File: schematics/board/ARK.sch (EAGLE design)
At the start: 85 parts, among them IC2 STM32F103C8T

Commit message: Готова схема платы АРК
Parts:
- removed 3,3µH: 3,3µ, CanCubeSat:B82472G6
- removed 3,3µH1: 3,3µH, CanCubeSat:B82472G6
- removed AD5272#2: AD5272, CanCubeSat:AD5272
- removed C29: 1µ, rcl:C-USC0603
- removed C3: 470nF, rcl:C-EUC0603
- removed C40, C41, C49, C50, C56: 0,1µ, rcl:C-USC0603
- removed C44, C52: 680p, rcl:C-USC0603
- removed C45, C53: 4.7µ, rcl:C-USC1206
- removed C46: 3,3n, rcl:C-USC0603
- removed C47, C54: 150µ, CanCubeSat:ECAPECAP150
- removed C48, C55: 220µ, CanCubeSat:ECAPECAP220
- removed C57: 10µ, rcl:C-USC1206
- removed INVERT: INVERTER., CanCubeSat:INVERTER.
- removed LED_G1, LED_G2, LED_R1, LED_R2: (no value), led:LEDCHIPLED_0603
- removed OPA: OPA333, CanCubeSat:OPA333
- removed R1: 91K, resistor:R-US_R0603
- removed R100, R32, R33, R57: 2k, resistor:R-US_R0603
- removed R28, R30, R67, R68, R69: 150k, resistor:R-US_R0603
- removed R3: 14K3, resistor:R-US_R0603
- removed R4: 120k, resistor:R-US_R0603
- removed R5: 430k, resistor:R-US_R0603
- removed R65: 1M, resistor:R-US_R0603
- removed R66: 10k, resistor:R-US_R0603
- removed R7: 680k, resistor:R-US_R0603
- removed REF3033: REF3033, CanCubeSat:REF3033
- removed U$1: MF-R400, CanCubeSat:MF-R400
- removed U$23, U$59: LTC31191, CanCubeSat:LTC31191
- removed VR-FB: 3314G-1-504E, CanCubeSat:3314G-1-504E
- removed VR-RUN: 3313J-1-205E, CanCubeSat:3313J-1-205E
- added 3362H, 3362H1: 20k, CanCubeSat:3362H
- added 3362P, 3362P1, 3362P4: 1k, CanCubeSat:3362P-1-502LF
- added 3362P2, 3362P5: 5k, CanCubeSat:3362P-1-502LF
- added 3362P3: 500R, CanCubeSat:3362P-1-502LF
- added C1.C, C1.D, C2B.C, C2B.D: 100nF, rcl:C-EUC0603
- added C2A.C, C2A.D: 22µF, rcl:C-EUC1206
- added C3.C, C3.D, C4A.C, C4A.D, C5.C, C5.D: 1µF, rcl:C-EUC0603
- added C4B.C, C4B.D: 1000µF, CanCubeSat:ECAPECAP1000
- added C6.C, C6.D: 10nF, rcl:C-EUC0603
- added C7.C, C7.D, C8.C, C8.D: (10nF), rcl:C-EUC0603
- added INVERT1: INVERTER., CanCubeSat:INVERTER.
- added L1.C, L1.D: 10µH, CanCubeSat:L_10MKH
- added OPA1, OPA2, OPA3: OPA333, CanCubeSat:OPA333
- added PB1, PB2, PB3, PB4, PB6, PB7: (no value), led:LEDCHIPLED_0603
- added R1.C, R1.D: 62k, rcl:R-US_R0603
- added R10, R12, R14, R15, R2, R21, R25, R29, R31, R34, R35, R36, R37, R38, R39, R40, R41, R42, R45, R48, R49, R6, R8, R9: 10k, resistor:R-US_R0603
- added R10.C, R10.D: 11k, rcl:R-US_R0603
- added R11: 34k8, resistor:R-US_R0603
- added R11.C, R11.D, R12.C, R12.D, R13.C, R13.D, R14.C, R14.D, R15.C, R15.D: 100k, rcl:R-US_R0603
- added R13: 91k, resistor:R-US_R0603
- added R16, R17, R18, R22, R23, R24, R26, R43: 2k, resistor:R-US_R0603
- added R16.C, R16.D, R17.C, R17.D, R2.C, R2.D, R6.C, R6.D: 10k, rcl:R-US_R0603
- added R18.C, R18.D: 51k, rcl:R-US_R0603
- added R19, R20: 51k, resistor:R-US_R0603
- added R19.C, R19.D: (1M), rcl:R-US_R0603
- added R44: 1k, resistor:R-US_R0603
- added R46: 24k9, resistor:R-US_R0603
- added R47: 620k, resistor:R-US_R0603
- added R5.C, R5.D: 191k, rcl:R-US_R0603
- added R7.C, R7.D: 17k8, rcl:R-US_R0603
- added R8.C, R8.D: (10k), rcl:R-US_R0603
- added R9.C, R9.D: 200k, rcl:R-US_R0603
- added ROZE1, ROZE2, ROZE3, ROZE4: (no value), pinheadCS:PINHD-1X2
- added U$10, U$11, U$17, U$18, U$19, U$22, U$24, U$25, U$27, U$28, U$30, U$31, U$32, U$33, U$41, U$42, U$43, U$46, U$47, U$48, U$50, U$51, U$53, U$9: VIAS, CanCubeSat:VIAS
- added U$13, U$14, U$15, U$16, U$20, U$21, U$26, U$29, U$39, U$40, U$44, U$45, U$49, U$52: VIAS-CONNECT, CanCubeSat:VIAS-CONNECT
- added U$2, U$5: MP5515, CanCubeSat:MP5515
- added U$34, U$35, U$6: IRF7329PBF, CanCubeSat:IRF7329PBF
- added U$36, U$37: IRF7905PBF, CanCubeSat:IRF7905PBF
- added U$38: SI2302CDS, CanCubeSat:SI2302CDS
- added U$7, U$8: SMP100LC-8, CanCubeSat:SMP100LC-8
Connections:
- removed net 3V3-STAB: IC2.VDDA, INVERT.VCC, OPA.V+, R4.1, REF3033.OUT
- removed net 90: R65.1, R66.2, R67.2, U$59.MPPC
- removed net DPD_RST: AD5272#2.RESET, IC2.PB15
- removed net GND-OUT: JP1.11, JP1.12, U$1.P$2, U$12.3, U$12.5, U$12.7, U$12.9
- removed net N$129: C41.2, U$59.BST2
- removed net N$131: 3,3µH.2, C40.1, U$59.SW1
- removed net N$132: 3,3µH.1, C41.1, U$59.SW2
- removed net N$135: R69.1, U$59.VC
- removed net N$136: C44.1, R69.2
- removed net N$139: C46.1, R66.1
- removed net N$142: R68.2, U$59.RT
- removed net N$144: C40.2, U$59.BST1
- removed net N$161: IC2.PB5, R81.1
- removed net N$2: OPA.IN+, R4.2, R5.2, R7.2
- removed net N$215: AD5272#2.VDD, C53.1, C56.1, C57.1, LED_G2.A, U$23.MPPC, U$23.SVCC, U$23.VCC
- removed net N$234: C45.1, LED_G1.A, U$59.SVCC, U$59.VCC
- removed net N$3: AD5272#2.A, R1.2, U$23.FB
- removed net N$48: AD5272#2.VSS, AD5272#2.W, C29.2, R3.1
- removed net N$51: AD5272#2.CAP, C29.1
- removed net N$77: 3,3µH1.2, C49.1, U$23.SW1
- removed net N$78: 3,3µH1.1, C50.1, U$23.SW2
- removed net N$79: R28.2, U$23.RT
- removed net N$80: C49.2, U$23.BST1
- removed net N$81: R30.1, U$23.VC
- removed net N$82: C52.1, R30.2
- removed net N$84: C50.2, U$23.BST2
- removed net N$85: LED_R1.A, R32.2
- removed net N$87: LED_R2.A, R57.2
- removed net N$89: U$59.FB, VR-FB.WIPER
- removed net N$91: LED_G1.C, R100.2
- removed net N$92: LED_G2.C, R33.2
- removed net PGOOD1: IC2.PB1, LED_R2.C, U$59.PGOOD
- removed net PGOOD2: IC2.PB0, LED_R1.C, U$23.PGOOD
- removed net RUN: OPA.IN-, VR-RUN.WIPER
- new net 0V8: 3362P.WIPER, OPA2.IN+, U$32.1
- new net AGND: C1.C.1, C1.D.1, C3.C.2, C3.D.2, C6.C.2, C6.D.2, C7.C.2, C7.D.2, C8.C.2, C8.D.2, R10.C.2, R10.D.2, R13.C.1, R13.D.1, R18.C.2, R18.D.2, R19.C.2, R19.D.2, R2.C.2, R2.D.2, R6.C.2, R6.D.2, R7.C.1, R7.D.1, U$2.AGND, U$39.2, U$5.AGND
- new net DC-DC: IC2.PA15, R42.2, U$38.G
- new net FBB-C: R15.2, U$2.FBB
- new net FBB-D: R25.2, U$5.FBB
- new net INT-C: IC2.PB4, R15.C.1, U$2.INT
- new net INT-D: IC2.PA8, R15.D.1, U$5.INT
- new net LED: IC2.PB0, R81.1
- new net N$10: R1.C.2, R2.C.1, U$2.DET
- new net N$100: 3362P5.WIPER, OPA1.IN-, U$48.1
- new net N$101: R45.2, U$44.1, U$47.1
- new net N$102: R46.1, U$45.2, U$46.1
- new net N$104: 3362H1.CCW, R48.1
- new net N$105: 3362H1.WIPER, OPA1.IN+, U$51.1
- new net N$106: 3362H1.CW, R47.2
- new net N$108: R47.1, U$49.2, U$50.1
- new net N$109: R48.2, U$52.2, U$53.1
- new net N$11: R10.C.1, R9.C.2, U$2.OVP
- new net N$12: C8.C.1, U$2.DVDT
- new net N$13: R18.C.1, U$2.ICH
- new net N$15: R19.C.1, U$2.TEMP
- new net N$16: R13.C.2, U$2.SAS
- new net N$18: C6.C.1, U$2.CST
- new net N$19: C4A.C.2, C4B.C.1, R5.C.1, R8.C.1, U$2.STRG
- new net N$20: C5.C.2, U$2.BST
- new net N$21: C5.C.1, L1.C.1, U$2.SW
- new net N$22: R5.C.2, R6.C.1, U$2.FBS
- new net N$23: R8.C.2, U$2.RTEST
- new net N$24: 3362P4.CCW, R22.1
- new net N$25: R29.2, U$36.D1, U$6.G1
- new net N$26: R17.C.1, U$2.SCL
- new net N$27: R16.C.1, U$2.SDA
- new net N$28: R35.2, U$34.G, U$37.D
- new net N$29: 3362P2.WIPER, OPA3.IN+, U$19.1
- new net N$30: R11.D.1, R12.D.2, U$5.EN
- new net N$31: R1.D.2, R2.D.1, U$5.DET
- new net N$32: R10.D.1, R9.D.2, U$5.OVP
- new net N$33: R7.D.2, U$5.ILIM
- new net N$34: C7.D.1, U$5.TPOR
- new net N$35: C8.D.1, U$5.DVDT
- new net N$36: R18.D.1, U$5.ICH
- new net N$37: R19.D.1, U$5.TEMP
- new net N$38: R13.D.2, U$5.SAS
- new net N$39: C6.D.1, U$5.CST
- new net N$40: C5.D.2, U$5.BST
- new net N$41: C5.D.1, L1.D.1, U$5.SW
- new net N$42: R5.D.2, R6.D.1, U$5.FBS
- new net N$43: R8.D.2, U$5.RTEST
- new net N$44: C4A.D.2, C4B.D.1, R5.D.1, R8.D.1, U$5.STRG
- new net N$46: U$35.D, U$35.D1
- new net N$47: R17.D.1, U$5.SCL
- new net N$49: R16.D.1, U$5.SDA
- new net N$5: R34.2, U$34.G1, U$37.D1
- new net N$52: OPA2.OUT, R15.1, U$29.1
- new net N$53: 3362H.WIPER, OPA2.IN-, U$28.1
- new net N$54: 3362H.CW, R9.2
- new net N$55: 3362H.CCW, R10.1
- new net N$56: PB1.C, R16.2
- new net N$57: 3362P.CW, R11.1
- new net N$58: 3362P.CCW, R12.2
- new net N$59: 3362P1.CW, R13.1
- new net N$6: OPA3.OUT, R25.1, U$13.1
- new net N$60: 3362P1.CCW, R14.2
- new net N$61: 3362P1.WIPER, U$25.1, U$26.1
- new net N$62: 3362P2.CW, R20.1
- new net N$63: PB2.C, R17.2
- new net N$64: 3362P2.CCW, R21.2
- new net N$65: PB3.C, R18.2
- new net N$66: 3362P4.WIPER, OPA3.IN-, U$10.1
- new net N$67: 3362P4.CW, R19.2
- new net N$68: PB4.C, R23.2
- new net N$69: PB6.C, R24.2
- new net N$7: R11.C.1, R12.C.2, U$2.EN
- new net N$70: PB7.C, R26.2
- new net N$71: R22.2, U$13.2, U$9.1
- new net N$72: R19.1, U$11.1, U$14.2
- new net N$73: R20.2, U$15.1, U$18.1
- new net N$74: R21.1, U$16.2, U$17.1
- new net N$75: R13.2, U$21.2, U$24.1
- new net N$76: R14.1, U$20.1, U$22.1
- new net N$8: R7.C.2, U$2.ILIM
- new net N$83: R9.1, U$26.2, U$27.1
- new net N$86: R10.2, U$29.2, U$30.1
- new net N$88: R31.2, U$36.D, U$6.G
- new net N$9: C7.C.1, U$2.TPOR
- new net N$90: 3362P3.CW, R43.1
- new net N$93: 3362P3.CCW, R44.2
- new net N$94: 3362P3.WIPER, U$43.1, U$52.1
- new net N$95: R40.2, R41.2, U$35.G, U$35.G1, U$38.D
- new net N$96: R43.2, U$39.1, U$42.1
- new net N$97: R44.1, U$40.2, U$41.1
- new net N$98: 3362P5.CW, R45.1
- new net N$99: 3362P5.CCW, R46.2
- new net PFI-C: IC2.PB6, PB1.A, R14.C.2, U$2.PFI
- new net PFI-D: IC2.PB14, PB4.A, R14.D.2, U$5.PFI
- new net PGB-C: IC2.PB7, PB3.A, U$2.PGB
- new net PGB-D: IC2.PB15, PB7.A, U$5.PGB
- new net PGS-C: IC2.PB5, PB2.A, U$2.PGS
- new net PGS-D: IC2.PB13, PB6.A, U$5.PGS
- new net ROZE-1: IC2.PA7, R2.1, ROZE1.1
- new net ROZE-2: IC2.PB3, R6.1, ROZE2.1
- new net ROZE-3: IC2.PA11, R8.1, ROZE3.1
- new net ROZE-4: IC2.PB1, R49.1, ROZE4.1
- new net VB-C: C2A.C.1, C2B.C.1, R12.C.1, R31.1, U$2.VB, U$6.S
- new net VB-D: C2A.D.1, C2B.D.1, R12.D.1, R35.1, U$34.S, U$5.VB
- new net VBO-C: L1.C.2, U$2.VBO
- new net VBO-D: L1.D.2, U$5.VBO
- new net VCC-C: C3.C.1, R14.C.1, R15.C.2, R16.C.2, R17.C.2, U$2.VCC
- new net VCC-D: C3.D.1, R14.D.1, R15.D.2, R16.D.2, R17.D.2, U$5.VCC
- new net VIN-C: C1.C.2, R1.C.1, R11.C.2, R9.C.1, U$2.VIN, U$6.D1, U$7.C
- new net VIN-D: C1.D.2, R1.D.1, R11.D.2, R9.D.1, U$34.D1, U$5.VIN, U$8.C
- net 1W: now also IC2.PA5; no longer IC2.PA7
- net 3V3: now also IC2.VDDA, INVERT1.VCC, OPA1.V+, OPA2.V+, OPA3.V+, R11.2, R2.2, R49.2, R6.2, R8.2, U$31.1, U$40.1
- net A: now also INVERT1.A, OPA1.OUT, R38.2, R39.2, U$37.G, U$37.G1, U$49.1; no longer INVERT.A, OPA.OUT, R32.1, R7.1, U$23.RUN
- net BMS+: now also R34.1, R40.1, U$14.1, U$34.S1, U$35.S1, U$6.D; no longer C3.2, REF3033.IN
- net BMS1: now also IC2.PA1; no longer IC2.PA6
- net BMS2: now also IC2.PA2; no longer IC2.PA5
- net BMS3: now also IC2.PC15; no longer IC2.PA4
- net BMS4: now also IC2.PA0-WKUP; no longer IC2.PA3
- net BMS5: now also IC2.PC13; no longer IC2.PA2
- net BMS6: now also IC2.PC14; no longer IC2.PA1
- net BUS+: now also R29.1, R41.1, U$15.2, U$21.1, U$34.D, U$35.S, U$45.1, U$6.S1
- net GND: now also C2A.C.2, C2A.D.2, C2B.C.2, C2B.D.2, C4A.C.1, C4A.D.1, C4B.C.2, C4B.D.2, INVERT1.GND, JP1.11, JP1.12, OPA1.V-, OPA2.V-, OPA3.V-, R12.1, R16.1, R17.1, R18.1, R23.1, R24.1, R26.1, R36.1, R37.1, R38.1, R39.1, R42.1, ROZE1.2, ROZE2.2, ROZE3.2, ROZE4.2, U$12.3, U$12.5, U$12.7, U$12.9, U$16.1, U$20.2, U$33.1, U$36.S, U$36.S1, U$37.S, U$37.S1, U$38.S, U$44.2, U$7.A, U$8.A; no longer AD5272#2.ADDR, AD5272#2.GND, C3.1, C44.2, C45.2, C46.2, C47.2, C48.2, C52.2, C53.2, C54.2, C55.2, C56.2, C57.2, IC2.PB2, INVERT.GND, OPA.V-, R100.1, R28.1, R3.2, R33.1, R5.1, R67.1, R68.1, REF3033.GND, U$1.P$1, U$23.PGND, U$23.PWM, U$23.SGND, U$59.PGND, U$59.PWM, U$59.SGND, VR-FB.CW, VR-RUN.CW
- net INA_BMS+: no longer C47.1, C55.1, U$23.PVIN, U$23.VIN, U$59.PVOUT, VR-FB.CCW
- net INA_BUS+: no longer C48.1, C54.1, R1.1, R65.2, U$23.PVOUT, U$59.PVIN, U$59.VIN, VR-RUN.CCW
- net SCL: no longer AD5272#2.SCL
- net SDA: no longer AD5272#2.SDA
- net TIME: now also IC2.PA3; no longer IC2.PB6
- net Y: now also INVERT1.Y, R36.2, R37.2, U$36.G, U$36.G1; no longer INVERT.Y, R57.1, U$59.RUN
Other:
- note added: "Выключатель АРКа"
- note removed: "Источник опорного напряжения 3V3-STUB"
- note removed: "Предохранитель и выключатель АРКа"
- moved on the sheet: C11, C4, LD1117S33, R101, R102, SWITCH

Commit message: Начата разводка платы АРК
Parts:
- C4A.C, C4A.D: device rcl:C-EUC0603 -> rcl:C-EUC1206
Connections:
- new net N$2: IC2.PB1
- new net N$3: IC2.PB2
- net 1W: now also IC2.PA4; no longer IC2.PA5
- net AGND: no longer C1.C.1, C1.D.1
- net BMS+: no longer R34.1, R40.1, U$34.S1, U$35.S1, U$6.D
- net BUS+: no longer R29.1, R41.1, U$34.D, U$35.S, U$6.S1
- net GND: now also C1.C.1, C1.D.1, U$2.PGND, U$5.PGND
- net INA_BMS+: now also R34.1, R40.1, U$34.S1, U$35.S1, U$6.D
- net INA_BUS+: now also R29.1, R41.1, U$34.D, U$35.S, U$6.S1
- net INT-C: now also IC2.PB13; no longer IC2.PB4
- net INT-D: now also IC2.PB4; no longer IC2.PA8
- net LED: now also IC2.PB12; no longer IC2.PB0
- net PFI-C: now also IC2.PA8; no longer IC2.PB6
- net PFI-D: now also IC2.PB7; no longer IC2.PB14
- net PGB-C: now also IC2.PB14; no longer IC2.PB7
- net PGB-D: now also IC2.PB6; no longer IC2.PB15
- net PGS-C: now also IC2.PB15; no longer IC2.PB5
- net PGS-D: now also IC2.PB5; no longer IC2.PB13
- net ROZE-1: now also IC2.PA5; no longer IC2.PA7
- net ROZE-2: now also IC2.PA6; no longer IC2.PB3
- net ROZE-3: now also IC2.PA7; no longer IC2.PA11
- net ROZE-4: now also IC2.PB0; no longer IC2.PB1

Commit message: Разведена плата АРК
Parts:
- removed C15: 100nF, rcl:C-EUC0603
- removed R36, R37: 10k, resistor:R-US_R0603
- added R1: 10k, resistor:R-US_R0603
- added R3: 100, resistor:R-US_R0603
- R39: value 10k -> 100
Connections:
- removed net N$2: IC2.PB1
- removed net N$3: IC2.PB2
- new net C-OFF: IC2.PB1, R3.1
- new net D-OFF: IC2.PB2, R39.2
- new net N$48: R1.2, R3.2, U$36.G1, U$36.G2
- new net N$51: R38.1, R39.1, U$37.G1, U$37.G2
- net 3V3: no longer C15.1
- net A: no longer R39.2, U$37.G, U$37.G1
- net AGND: now also INVERT1.GND, OPA1.V-, OPA2.V-, OPA3.V-
- net GND: now also U$36.S2, U$37.S2; no longer C15.2, INVERT1.GND, OPA1.V-, OPA2.V-, OPA3.V-, R36.1, R37.1, R38.1, R39.1, U$36.S, U$37.S
- net INA_BMS+: now also U$34.S2, U$35.S2, U$6.D1; no longer U$34.S1, U$35.S1, U$6.D
- net INA_BUS+: now also U$34.D1, U$35.S1, U$6.S2; no longer U$34.D, U$35.S, U$6.S1
- net INT-D: now also IC2.PB5; no longer IC2.PB4
- net N$25: now also U$6.G2; no longer U$6.G1
- net N$28: now also U$34.G1, U$37.D2; no longer U$34.G, U$37.D
- net N$46: now also U$35.D2; no longer U$35.D
- net N$5: now also U$34.G2; no longer U$34.G1
- net N$88: now also U$36.D2, U$6.G1; no longer U$36.D, U$6.G
- net N$95: now also U$35.G2; no longer U$35.G
- net PFI-D: now also IC2.PB4; no longer IC2.PB7
- net PGS-D: now also IC2.PB7; no longer IC2.PB5
- net VB-C: now also U$6.S1; no longer U$6.S
- net VB-D: now also U$34.S1; no longer U$34.S
- net VIN-C: now also U$6.D2; no longer U$6.D1
- net VIN-D: now also U$34.D2; no longer U$34.D1
- net Y: now also R1.1; no longer R36.2, R37.2, U$36.G, U$36.G1
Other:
- moved on the sheet: C5, R38, R39

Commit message: Плата АРК готова
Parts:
- removed 3362H, 3362H1: 20k, CanCubeSat:3362H
- added 3362P6, 3362P7: 20k, CanCubeSat:3362P-1-502LF
- added R28, R4, R5, R7: 100, resistor:R-US_R0603
- added U$1: VIN-C, CanCubeSat:VIAS-CONNECTW1.4MM
- added U$23: VB-C, CanCubeSat:VIAS-CONNECTW1.4MM
- added U$54: VIN-D, CanCubeSat:VIAS-CONNECTW1.4MM
- added U$55: VB-D, CanCubeSat:VIAS-CONNECTW1.4MM
- U$10, U$28, U$48: value VIAS -> IN-
- U$11, U$17, U$18, U$22, U$24, U$27, U$30, U$41, U$42, U$46, U$47, U$50, U$53, U$9: value VIAS -> (none)
- U$13, U$29: value VIAS-CONNECT -> OUT
- U$14: value VIAS-CONNECT -> BMS+
- U$15, U$21, U$45: value VIAS-CONNECT -> BUS+
- U$16, U$20, U$39, U$44: value VIAS-CONNECT -> AGND
- U$19, U$32, U$51: value VIAS -> IN+
- U$25, U$43: value VIAS -> REF
- U$26, U$52: value VIAS-CONNECT -> REF
- U$31: value VIAS -> 3V3
- U$33: value VIAS -> AGND
- U$40: value VIAS-CONNECT -> 3V3
- U$49: value VIAS-CONNECT -> OUT-D
- renumbered PB1 to PFI-C, PB2 to PGS-C, PB3 to PGB-C, PB4 to PFI-D, PB5 to LED, PB6 to PGS-D, PB7 to PGB-D, U$7 to D$1, U$8 to D$2
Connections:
- new net N$2: U$1.1, U$6.D2
- new net N$3: R31.1, U$23.1, U$6.S1
- new net N$50: U$34.D2, U$54.1
- new net N$77: R35.1, U$34.S1, U$55.1
- new net N$78: R5.2, U$37.D2
- new net N$79: R28.1, U$36.D2
- new net N$80: R4.2, U$37.D1
- new net N$81: R7.1, U$36.D1
- net AGND: now also R12.1, U$16.1, U$20.2, U$33.1, U$44.2
- net GND: no longer R12.1, U$16.1, U$20.2, U$33.1, U$44.2
- net N$104: now also 3362P7.CCW; no longer 3362H1.CCW
- net N$105: now also 3362P7.WIPER; no longer 3362H1.WIPER
- net N$106: now also 3362P7.CW; no longer 3362H1.CW
- net N$25: now also R7.2; no longer U$36.D1
- net N$28: now also R5.1; no longer U$37.D2
- net N$5: now also R4.1; no longer U$37.D1
- net N$53: now also 3362P6.WIPER; no longer 3362H.WIPER
- net N$54: now also 3362P6.CW; no longer 3362H.CW
- net N$55: now also 3362P6.CCW; no longer 3362H.CCW
- net N$88: now also R28.2; no longer U$36.D2
- net VB-C: now also U$23.2; no longer R31.1, U$6.S1
- net VB-D: now also U$55.2; no longer R35.1, U$34.S1
- net VIN-C: now also U$1.2; no longer U$6.D2
- net VIN-D: now also U$54.2; no longer U$34.D2

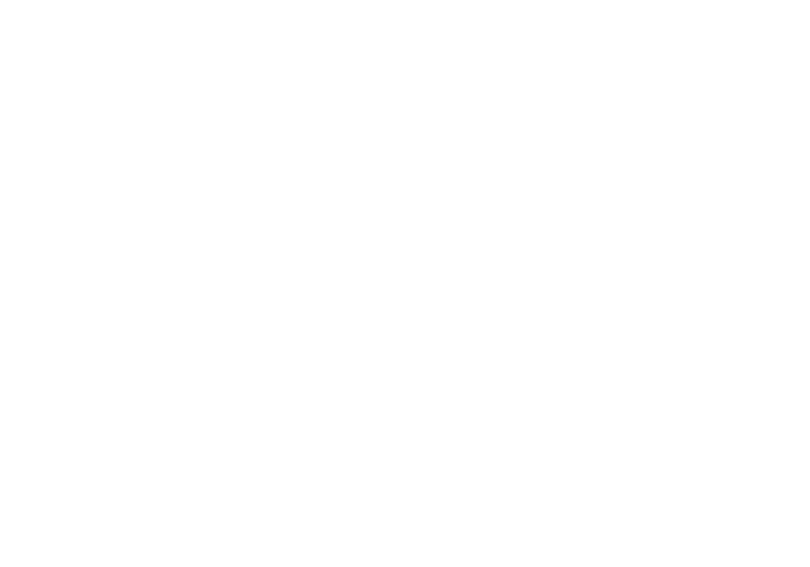
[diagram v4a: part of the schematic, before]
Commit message: Забыл объединить земли на плате АРК. Исправился
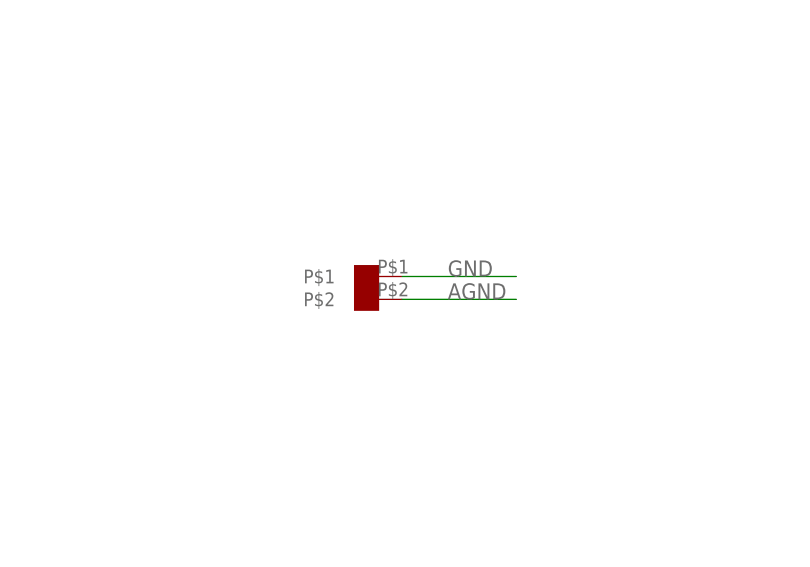
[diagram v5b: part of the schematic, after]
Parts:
- added U$7: GNDS-CONNECTOR, CanCubeSat:GNDS-CONNECTOR
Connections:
- net AGND: now also U$7.P$2
- net GND: now also U$7.P$1
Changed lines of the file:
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@@
 <part name="3362P6" library="CanCubeSat" deviceset="3362P-1-502LF" device="" value="20k"/>
 <part name="3362P7" library="CanCubeSat" deviceset="3362P-1-502LF" device="" value="20k"/>
+<part name="U$7" library="CanCubeSat" deviceset="GNDS-CONNECTOR" device=""/>
 </parts>
 <sheets>
@@
 <attribute name="VALUE" x="375.9245" y="55.902259375" size="1.7848" layer="96" rot="R180"/>
 </instance>
+<instance part="U$7" gate="G$1" x="-210.82" y="426.72" smashed="yes"/>
 </instances>
 <busses>
@@
 <wire x1="-50.8" y1="73.66" x2="-50.8" y2="55.88" width="0.1524" layer="91"/>
 <label x="-50.8" y="55.88" size="1.778" layer="95" rot="R90"/>
+</segment>
+<segment>
+<pinref part="U$7" gate="G$1" pin="P$1"/>
+<wire x1="-203.2" y1="426.72" x2="-190.5" y2="426.72" width="0.1524" layer="91"/>
+<label x="-198.12" y="426.72" size="1.778" layer="95"/>
 </segment>
 </net>
@@
 <junction x="-340.36" y="-81.28"/>
 </segment>
-</net>
+<segment>
+<pinref part="U$7" gate="G$1" pin="P$2"/>
+<wire x1="-203.2" y1="424.18" x2="-190.5" y2="424.18" width="0.1524" layer="91"/>
+<label x="-198.12" y="424.18" size="1.778" layer="95"/>
+</segment>
+</net>
